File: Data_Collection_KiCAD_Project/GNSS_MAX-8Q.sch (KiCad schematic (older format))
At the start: 13 parts

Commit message: Fixed Component Libraries
Changed over from project specific to global libraries.
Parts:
- C? (x6): symbol Data_Collection_KiCAD_Project-rescue:C-Device -> Data_Collection_KiCAD_Project-rescue:C-Device-Data_Collection_KiCAD_Project-rescue
- J?: symbol Data_Collection_KiCAD_Project-rescue:Conn_Coaxial-Connector -> Data_Collection_KiCAD_Project-rescue:Conn_Coaxial-Connector-Data_Collection_KiCAD_Project-rescue
- L?: symbol Data_Collection_KiCAD_Project-rescue:L-Device -> Data_Collection_KiCAD_Project-rescue:L-Device-Data_Collection_KiCAD_Project-rescue
- Q?: symbol Data_Collection_KiCAD_Project-rescue:FDC6330L-Transistor_FET -> Data_Collection_KiCAD_Project-rescue:FDC6330L-Transistor_FET-Data_Collection_KiCAD_Project-rescue
- R? (x3): symbol Data_Collection_KiCAD_Project-rescue:R-Device -> Data_Collection_KiCAD_Project-rescue:R-Device-Data_Collection_KiCAD_Project-rescue
- U?: symbol Data_Collection_KiCAD_Project-rescue:MAX-8Q-RF_GPS -> Data_Collection_KiCAD_Project-rescue:MAX-8Q-RF_GPS-Data_Collection_KiCAD_Project-rescue
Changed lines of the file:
@@
 $Descr A4 11693 8268
 encoding utf-8
-Sheet 4 10
+Sheet 4 9
 Title "MAX-8Q GNSS Module"
 Date "2021-10-01"
@@
 $EndDescr
 $Comp
-L Data_Collection_KiCAD_Project-rescue:L-Device L?
+L Data_Collection_KiCAD_Project-rescue:L-Device-Data_Collection_KiCAD_Project-rescue L?
 U 1 1 616192D0
 P 3650 5950
@@
 $EndComp
 $Comp
-L Data_Collection_KiCAD_Project-rescue:GND-power #PWR?
+L Data_Collection_KiCAD_Project-rescue:GND-power-Data_Collection_KiCAD_Project-rescue #PWR?
 U 1 1 616192D6
 P 4000 6500
@@
 $EndComp
 $Comp
-L Data_Collection_KiCAD_Project-rescue:C-Device C?
+L Data_Collection_KiCAD_Project-rescue:C-Device-Data_Collection_KiCAD_Project-rescue C?
 U 1 1 616192DC
 P 4900 5550
@@
 $EndComp
 $Comp
-L Data_Collection_KiCAD_Project-rescue:R-Device R?
+L Data_Collection_KiCAD_Project-rescue:R-Device-Data_Collection_KiCAD_Project-rescue R?
 U 1 1 616192E2
 P 4700 5550
@@
 $EndComp
 $Comp
-L Data_Collection_KiCAD_Project-rescue:R-Device R?
+L Data_Collection_KiCAD_Project-rescue:R-Device-Data_Collection_KiCAD_Project-rescue R?
 U 1 1 616192E8
 P 4350 6250
@@
 $EndComp
 $Comp
-L Data_Collection_KiCAD_Project-rescue:FDC6330L-Transistor_FET Q?
+L Data_Collection_KiCAD_Project-rescue:FDC6330L-Transistor_FET-Data_Collection_KiCAD_Project-rescue Q?
 U 1 1 616192EF
 P 4000 5650
@@
 Connection ~ 4700 5350
 $Comp
-L Data_Collection_KiCAD_Project-rescue:GND-power #PWR?
+L Data_Collection_KiCAD_Project-rescue:GND-power-Data_Collection_KiCAD_Project-rescue #PWR?
 U 1 1 616192FE
 P 4900 5750
@@
 Connection ~ 4900 5350
 $Comp
-L Data_Collection_KiCAD_Project-rescue:R-Device R?
+L Data_Collection_KiCAD_Project-rescue:R-Device-Data_Collection_KiCAD_Project-rescue R?
 U 1 1 61619311
 P 3650 5550
@@
 	5500 6750 3000 6750
 $Comp
-L Data_Collection_KiCAD_Project-rescue:+3.3V-power #PWR?
+L Data_Collection_KiCAD_Project-rescue:+3.3V-power-Data_Collection_KiCAD_Project-rescue #PWR?
 U 1 1 6161C95B
 P 7200 2400
@@
 Connection ~ 7600 2450
 $Comp
-L Data_Collection_KiCAD_Project-rescue:GND-power #PWR?
+L Data_Collection_KiCAD_Project-rescue:GND-power-Data_Collection_KiCAD_Project-rescue #PWR?
 U 1 1 6161C967
 P 7700 3900
@@
 Connection ~ 7500 2450
 $Comp
-L Data_Collection_KiCAD_Project-rescue:Conn_Coaxial-Connector J?
+L Data_Collection_KiCAD_Project-rescue:Conn_Coaxial-Connector-Data_Collection_KiCAD_Project-rescue J?
 U 1 1 6161C976
 P 9400 3200
@@
 MAX-8Q: GNSS Module Chip
 $Comp
-L Data_Collection_KiCAD_Project-rescue:GND-power #PWR?
+L Data_Collection_KiCAD_Project-rescue:GND-power-Data_Collection_KiCAD_Project-rescue #PWR?
 U 1 1 6161C998
 P 1200 1950
@@
 $EndComp
 $Comp
-L Data_Collection_KiCAD_Project-rescue:C-Device C?
+L Data_Collection_KiCAD_Project-rescue:C-Device-Data_Collection_KiCAD_Project-rescue C?
 U 1 1 6161C99E
 P 1200 1700
@@
 $EndComp
 $Comp
-L Data_Collection_KiCAD_Project-rescue:+3.3V-power #PWR?
+L Data_Collection_KiCAD_Project-rescue:+3.3V-power-Data_Collection_KiCAD_Project-rescue #PWR?
 U 1 1 6161C9A4
 P 1200 1450
@@
 	1200 1450 1200 1500
 $Comp
-L Data_Collection_KiCAD_Project-rescue:C-Device C?
+L Data_Collection_KiCAD_Project-rescue:C-Device-Data_Collection_KiCAD_Project-rescue C?
 U 1 1 6161C9AC
 P 1600 1700
@@
 $EndComp
 $Comp
-L Data_Collection_KiCAD_Project-rescue:C-Device C?
+L Data_Collection_KiCAD_Project-rescue:C-Device-Data_Collection_KiCAD_Project-rescue C?
 U 1 1 6161C9B2
 P 2050 1700
@@
 $EndComp
 $Comp
-L Data_Collection_KiCAD_Project-rescue:C-Device C?
+L Data_Collection_KiCAD_Project-rescue:C-Device-Data_Collection_KiCAD_Project-rescue C?
 U 1 1 6161C9B8
 P 2500 1700
@@
 	1600 1900 2050 1900
 $Comp
-L Data_Collection_KiCAD_Project-rescue:C-Device C?
+L Data_Collection_KiCAD_Project-rescue:C-Device-Data_Collection_KiCAD_Project-rescue C?
 U 1 1 6161C9D2
 P 2950 1700
@@
 GPS_LNA_EN
 $Comp
-L Data_Collection_KiCAD_Project-rescue:GND-power #PWR?
+L Data_Collection_KiCAD_Project-rescue:GND-power-Data_Collection_KiCAD_Project-rescue #PWR?
 U 1 1 61679BC7
 P 9400 3400
@@
 ~RESET
 $Comp
-L Data_Collection_KiCAD_Project-rescue:GND-power #PWR?
+L Data_Collection_KiCAD_Project-rescue:GND-power-Data_Collection_KiCAD_Project-rescue #PWR?
 U 1 1 6167BBB2
 P 6550 3700
@@
 	6550 3400 7100 3400
 $Comp
-L Data_Collection_KiCAD_Project-rescue:MAX-8Q-RF_GPS U?
+L Data_Collection_KiCAD_Project-rescue:MAX-8Q-RF_GPS-Data_Collection_KiCAD_Project-rescue U?
 U 1 1 6161C986
 P 7700 3200

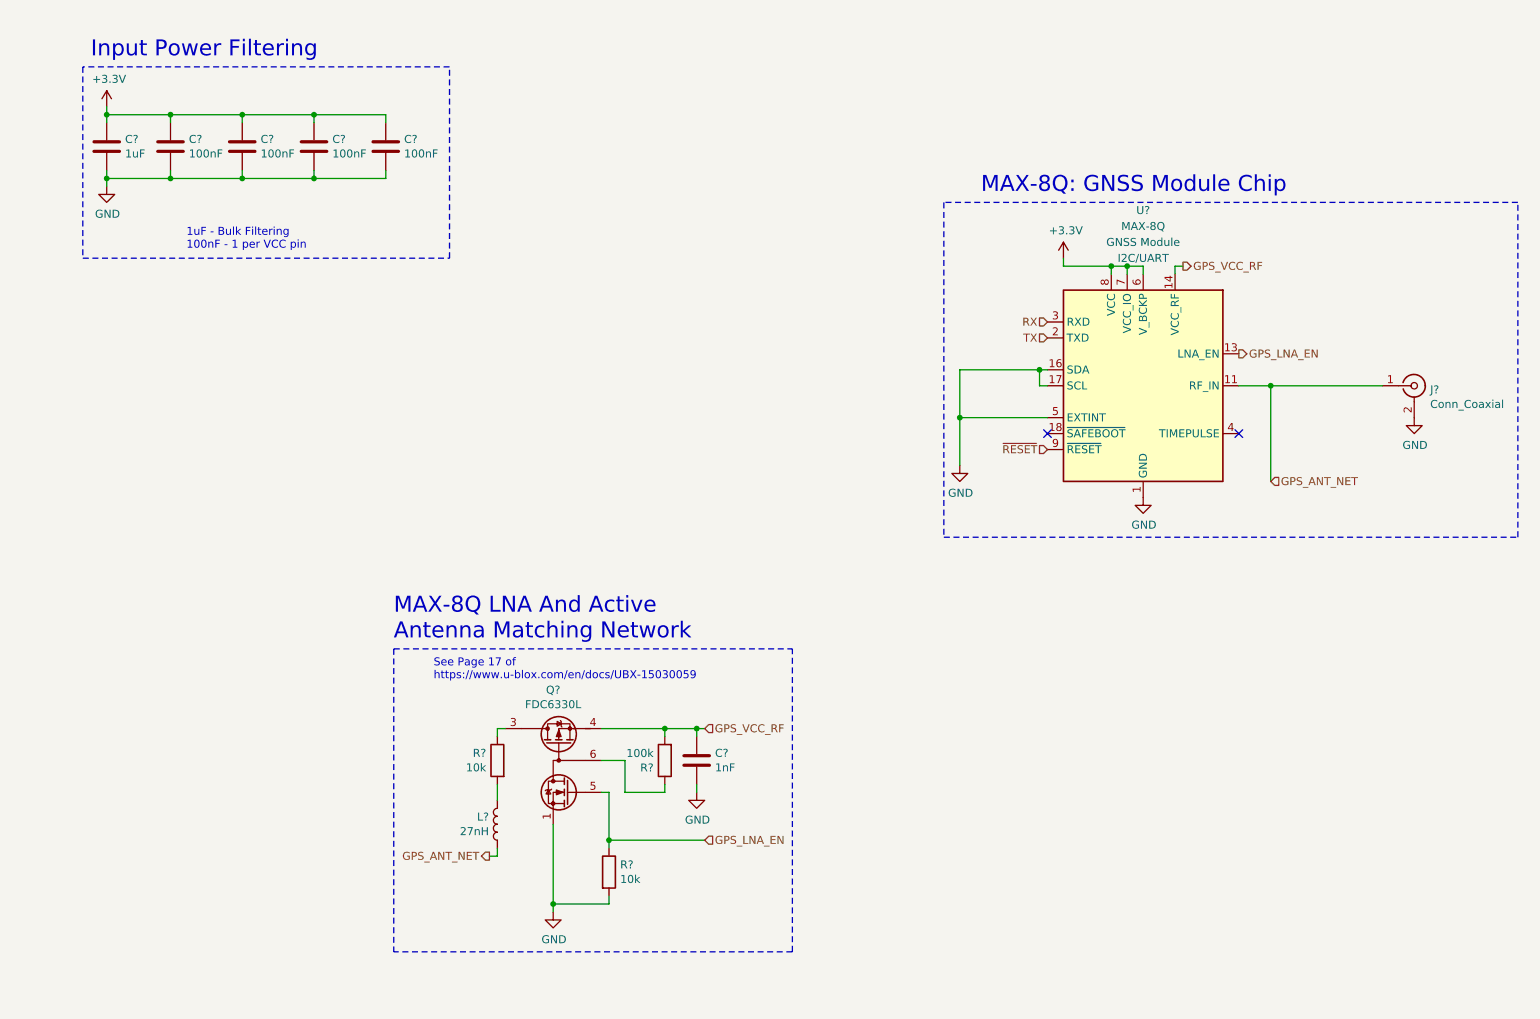
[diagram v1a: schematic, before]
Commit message: footprint and value changes
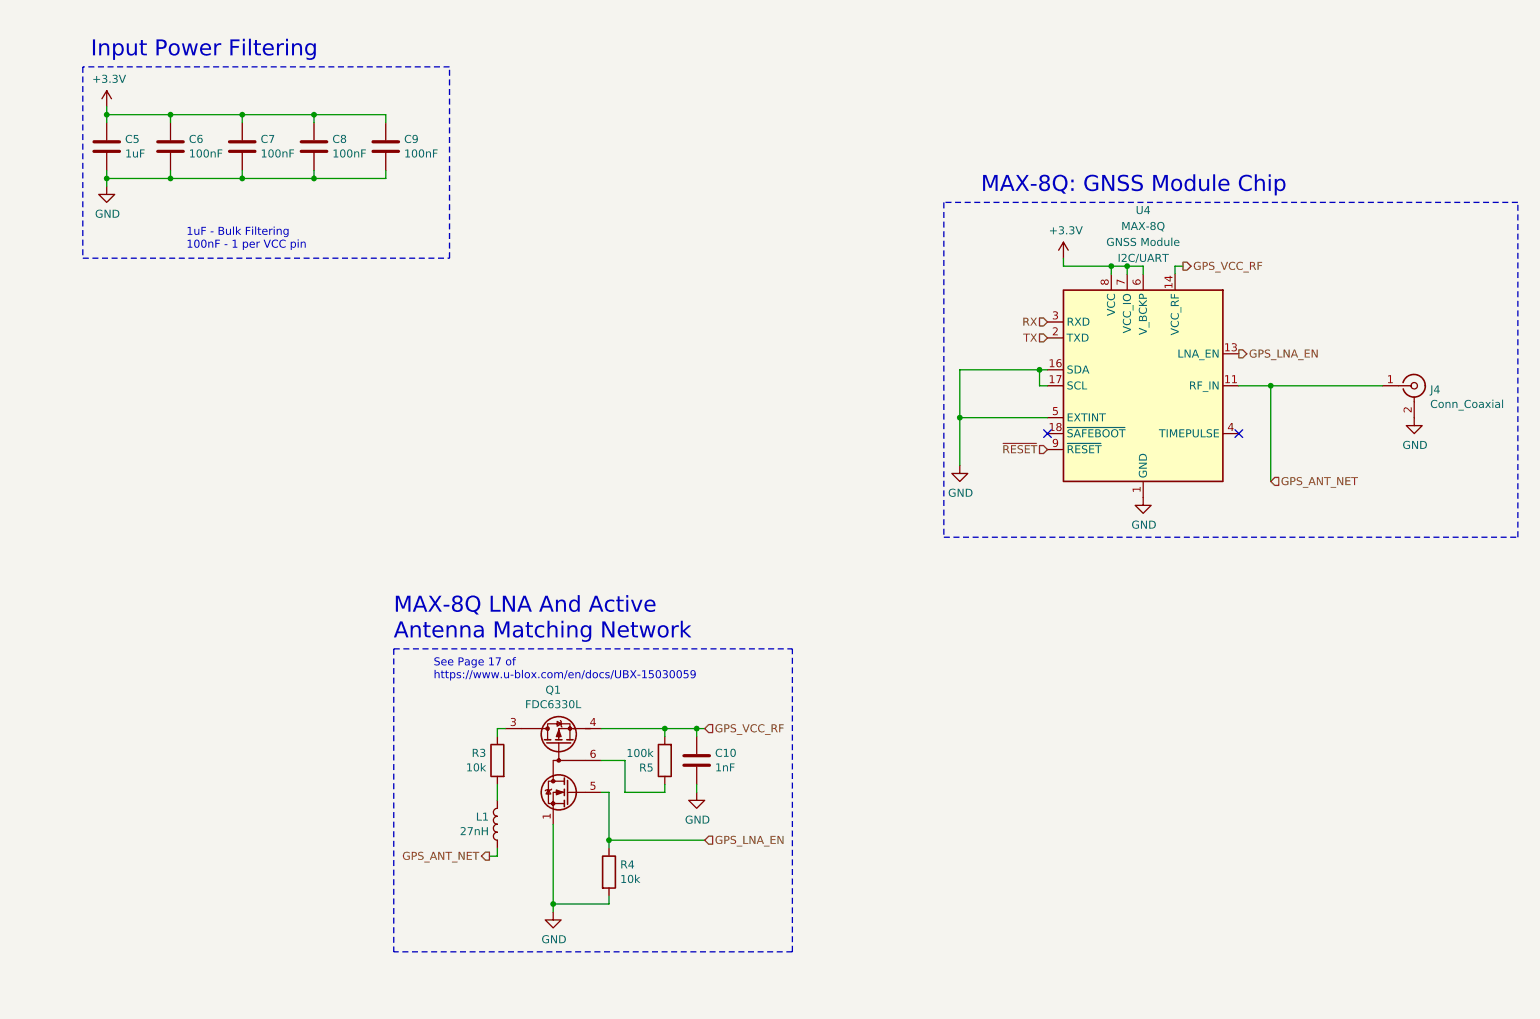
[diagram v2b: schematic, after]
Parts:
- C10, C5, C6, C7, C8, C9: renamed from C?; footprint (none) -> Capacitor_SMD:C_0603_1608Metric
- R3, R4, R5: renamed from R?; footprint (none) -> Resistor_SMD:R_0603_1608Metric
- gave numbers to parts that had none: 4
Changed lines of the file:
@@
 P 3650 5950
 AR Path="/616192D0" Ref="L?"  Part="1"
-AR Path="/615A5F2C/616192D0" Ref="L?"  Part="1"
-F 0 "L?" H 3703 5996 50  0000 L CNN
+AR Path="/615A5F2C/616192D0" Ref="L1"  Part="1"
+F 0 "L1" H 3703 5996 50  0000 L CNN
 F 1 "27nH" H 3703 5905 50  0000 L CNN
 F 2 "" H 3650 5950 50  0001 C CNN
@@
 P 4000 6500
 AR Path="/616192D6" Ref="#PWR?"  Part="1"
-AR Path="/615A5F2C/616192D6" Ref="#PWR?"  Part="1"
-F 0 "#PWR?" H 4000 6250 50  0001 C CNN
+AR Path="/615A5F2C/616192D6" Ref="#PWR025"  Part="1"
+F 0 "#PWR025" H 4000 6250 50  0001 C CNN
 F 1 "GND" H 4005 6327 50  0000 C CNN
 F 2 "" H 4000 6500 50  0001 C CNN
@@
 P 4900 5550
 AR Path="/616192DC" Ref="C?"  Part="1"
-AR Path="/615A5F2C/616192DC" Ref="C?"  Part="1"
-F 0 "C?" H 5015 5596 50  0000 L CNN
+AR Path="/615A5F2C/616192DC" Ref="C10"  Part="1"
+F 0 "C10" H 5015 5596 50  0000 L CNN
 F 1 "1nF" H 5015 5505 50  0000 L CNN
-F 2 "" H 4938 5400 50  0001 C CNN
+F 2 "Capacitor_SMD:C_0603_1608Metric" H 4938 5400 50  0001 C CNN
 F 3 "~" H 4900 5550 50  0001 C CNN
 	1    4900 5550
@@
 P 4700 5550
 AR Path="/616192E2" Ref="R?"  Part="1"
-AR Path="/615A5F2C/616192E2" Ref="R?"  Part="1"
-F 0 "R?" H 4770 5596 50  0000 L CNN
+AR Path="/615A5F2C/616192E2" Ref="R5"  Part="1"
+F 0 "R5" H 4770 5596 50  0000 L CNN
 F 1 "100k" H 4770 5505 50  0000 L CNN
-F 2 "" V 4630 5550 50  0001 C CNN
+F 2 "Resistor_SMD:R_0603_1608Metric" V 4630 5550 50  0001 C CNN
 F 3 "~" H 4700 5550 50  0001 C CNN
 	1    4700 5550
@@
 P 4350 6250
 AR Path="/616192E8" Ref="R?"  Part="1"
-AR Path="/615A5F2C/616192E8" Ref="R?"  Part="1"
-F 0 "R?" H 4420 6296 50  0000 L CNN
+AR Path="/615A5F2C/616192E8" Ref="R4"  Part="1"
+F 0 "R4" H 4420 6296 50  0000 L CNN
 F 1 "10k" H 4420 6205 50  0000 L CNN
-F 2 "" V 4280 6250 50  0001 C CNN
+F 2 "Resistor_SMD:R_0603_1608Metric" V 4280 6250 50  0001 C CNN
 F 3 "~" H 4350 6250 50  0001 C CNN
 	1    4350 6250
@@
 P 4000 5650
 AR Path="/616192EF" Ref="Q?"  Part="1"
-AR Path="/615A5F2C/616192EF" Ref="Q?"  Part="1"
-F 0 "Q?" H 4000 6192 50  0000 C CNN
+AR Path="/615A5F2C/616192EF" Ref="Q1"  Part="1"
+F 0 "Q1" H 4000 6192 50  0000 C CNN
 F 1 "FDC6330L" H 4000 6101 50  0000 C CNN
 F 2 "Package_TO_SOT_SMD:TSOT-23-6" H 3950 5075 50  0001 C CNN
@@
 P 4900 5750
 AR Path="/616192FE" Ref="#PWR?"  Part="1"
-AR Path="/615A5F2C/616192FE" Ref="#PWR?"  Part="1"
-F 0 "#PWR?" H 4900 5500 50  0001 C CNN
+AR Path="/615A5F2C/616192FE" Ref="#PWR026"  Part="1"
+F 0 "#PWR026" H 4900 5500 50  0001 C CNN
 F 1 "GND" H 4905 5577 50  0000 C CNN
 F 2 "" H 4900 5750 50  0001 C CNN
@@
 P 3650 5550
 AR Path="/61619311" Ref="R?"  Part="1"
-AR Path="/615A5F2C/61619311" Ref="R?"  Part="1"
-F 0 "R?" H 3720 5596 50  0000 L CNN
+AR Path="/615A5F2C/61619311" Ref="R3"  Part="1"
+F 0 "R3" H 3720 5596 50  0000 L CNN
 F 1 "10k" H 3720 5505 50  0000 L CNN
-F 2 "" V 3580 5550 50  0001 C CNN
+F 2 "Resistor_SMD:R_0603_1608Metric" V 3580 5550 50  0001 C CNN
 F 3 "~" H 3650 5550 50  0001 C CNN
 	1    3650 5550
@@
 P 7200 2400
 AR Path="/6161C95B" Ref="#PWR?"  Part="1"
-AR Path="/615A5F2C/6161C95B" Ref="#PWR?"  Part="1"
-F 0 "#PWR?" H 7200 2250 50  0001 C CNN
+AR Path="/615A5F2C/6161C95B" Ref="#PWR028"  Part="1"
+F 0 "#PWR028" H 7200 2250 50  0001 C CNN
 F 1 "+3.3V" H 7215 2573 50  0000 C CNN
 F 2 "" H 7200 2400 50  0001 C CNN
@@
 P 7700 3900
 AR Path="/6161C967" Ref="#PWR?"  Part="1"
-AR Path="/615A5F2C/6161C967" Ref="#PWR?"  Part="1"
-F 0 "#PWR?" H 7700 3650 50  0001 C CNN
+AR Path="/615A5F2C/6161C967" Ref="#PWR029"  Part="1"
+F 0 "#PWR029" H 7700 3650 50  0001 C CNN
 F 1 "GND" H 7705 3727 50  0000 C CNN
 F 2 "" H 7700 3900 50  0001 C CNN
@@
 P 9400 3200
 AR Path="/6161C976" Ref="J?"  Part="1"
-AR Path="/615A5F2C/6161C976" Ref="J?"  Part="1"
-F 0 "J?" H 9500 3175 50  0000 L CNN
+AR Path="/615A5F2C/6161C976" Ref="J4"  Part="1"
+F 0 "J4" H 9500 3175 50  0000 L CNN
 F 1 "Conn_Coaxial" H 9500 3084 50  0000 L CNN
 F 2 "" H 9400 3200 50  0001 C CNN
@@
 P 1200 1950
 AR Path="/6161C998" Ref="#PWR?"  Part="1"
-AR Path="/615A5F2C/6161C998" Ref="#PWR?"  Part="1"
-F 0 "#PWR?" H 1200 1700 50  0001 C CNN
+AR Path="/615A5F2C/6161C998" Ref="#PWR024"  Part="1"
+F 0 "#PWR024" H 1200 1700 50  0001 C CNN
 F 1 "GND" H 1205 1777 50  0000 C CNN
 F 2 "" H 1200 1950 50  0001 C CNN
@@
 P 1200 1700
 AR Path="/6161C99E" Ref="C?"  Part="1"
-AR Path="/615A5F2C/6161C99E" Ref="C?"  Part="1"
-F 0 "C?" H 1315 1746 50  0000 L CNN
+AR Path="/615A5F2C/6161C99E" Ref="C5"  Part="1"
+F 0 "C5" H 1315 1746 50  0000 L CNN
 F 1 "1uF" H 1315 1655 50  0000 L CNN
-F 2 "" H 1238 1550 50  0001 C CNN
+F 2 "Capacitor_SMD:C_0603_1608Metric" H 1238 1550 50  0001 C CNN
 F 3 "~" H 1200 1700 50  0001 C CNN
 	1    1200 1700
@@
 P 1200 1450
 AR Path="/6161C9A4" Ref="#PWR?"  Part="1"
-AR Path="/615A5F2C/6161C9A4" Ref="#PWR?"  Part="1"
-F 0 "#PWR?" H 1200 1300 50  0001 C CNN
+AR Path="/615A5F2C/6161C9A4" Ref="#PWR023"  Part="1"
+F 0 "#PWR023" H 1200 1300 50  0001 C CNN
 F 1 "+3.3V" H 1215 1623 50  0000 C CNN
 F 2 "" H 1200 1450 50  0001 C CNN
@@
 P 1600 1700
 AR Path="/6161C9AC" Ref="C?"  Part="1"
-AR Path="/615A5F2C/6161C9AC" Ref="C?"  Part="1"
-F 0 "C?" H 1715 1746 50  0000 L CNN
+AR Path="/615A5F2C/6161C9AC" Ref="C6"  Part="1"
+F 0 "C6" H 1715 1746 50  0000 L CNN
 F 1 "100nF" H 1715 1655 50  0000 L CNN
-F 2 "" H 1638 1550 50  0001 C CNN
+F 2 "Capacitor_SMD:C_0603_1608Metric" H 1638 1550 50  0001 C CNN
 F 3 "~" H 1600 1700 50  0001 C CNN
 	1    1600 1700
@@
 P 2050 1700
 AR Path="/6161C9B2" Ref="C?"  Part="1"
-AR Path="/615A5F2C/6161C9B2" Ref="C?"  Part="1"
-F 0 "C?" H 2165 1746 50  0000 L CNN
+AR Path="/615A5F2C/6161C9B2" Ref="C7"  Part="1"
+F 0 "C7" H 2165 1746 50  0000 L CNN
 F 1 "100nF" H 2165 1655 50  0000 L CNN
-F 2 "" H 2088 1550 50  0001 C CNN
+F 2 "Capacitor_SMD:C_0603_1608Metric" H 2088 1550 50  0001 C CNN
 F 3 "~" H 2050 1700 50  0001 C CNN
 	1    2050 1700
@@
 P 2500 1700
 AR Path="/6161C9B8" Ref="C?"  Part="1"
-AR Path="/615A5F2C/6161C9B8" Ref="C?"  Part="1"
-F 0 "C?" H 2615 1746 50  0000 L CNN
+AR Path="/615A5F2C/6161C9B8" Ref="C8"  Part="1"
+F 0 "C8" H 2615 1746 50  0000 L CNN
 F 1 "100nF" H 2615 1655 50  0000 L CNN
-F 2 "" H 2538 1550 50  0001 C CNN
+F 2 "Capacitor_SMD:C_0603_1608Metric" H 2538 1550 50  0001 C CNN
 F 3 "~" H 2500 1700 50  0001 C CNN
 	1    2500 1700
@@
 P 2950 1700
 AR Path="/6161C9D2" Ref="C?"  Part="1"
-AR Path="/615A5F2C/6161C9D2" Ref="C?"  Part="1"
-F 0 "C?" H 3065 1746 50  0000 L CNN
+AR Path="/615A5F2C/6161C9D2" Ref="C9"  Part="1"
+F 0 "C9" H 3065 1746 50  0000 L CNN
 F 1 "100nF" H 3065 1655 50  0000 L CNN
-F 2 "" H 2988 1550 50  0001 C CNN
+F 2 "Capacitor_SMD:C_0603_1608Metric" H 2988 1550 50  0001 C CNN
 F 3 "~" H 2950 1700 50  0001 C CNN
 	1    2950 1700
@@
 P 9400 3400
 AR Path="/61679BC7" Ref="#PWR?"  Part="1"
-AR Path="/615A5F2C/61679BC7" Ref="#PWR?"  Part="1"
-F 0 "#PWR?" H 9400 3150 50  0001 C CNN
+AR Path="/615A5F2C/61679BC7" Ref="#PWR030"  Part="1"
+F 0 "#PWR030" H 9400 3150 50  0001 C CNN
 F 1 "GND" H 9405 3227 50  0000 C CNN
 F 2 "" H 9400 3400 50  0001 C CNN
@@
 P 6550 3700
 AR Path="/6167BBB2" Ref="#PWR?"  Part="1"
-AR Path="/615A5F2C/6167BBB2" Ref="#PWR?"  Part="1"
-F 0 "#PWR?" H 6550 3450 50  0001 C CNN
+AR Path="/615A5F2C/6167BBB2" Ref="#PWR027"  Part="1"
+F 0 "#PWR027" H 6550 3450 50  0001 C CNN
 F 1 "GND" H 6555 3527 50  0000 C CNN
 F 2 "" H 6550 3700 50  0001 C CNN
@@
 P 7700 3200
 AR Path="/6161C986" Ref="U?"  Part="1"
-AR Path="/615A5F2C/6161C986" Ref="U?"  Part="1"
-F 0 "U?" H 7700 4300 50  0000 C CNN
+AR Path="/615A5F2C/6161C986" Ref="U4"  Part="1"
+F 0 "U4" H 7700 4300 50  0000 C CNN
 F 1 "MAX-8Q" H 7700 4200 50  0000 C CNN
 F 2 "RF_GPS:ublox_MAX" H 8100 2550 50  0001 C CNN
